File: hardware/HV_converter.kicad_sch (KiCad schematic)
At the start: 26 parts, among them J6 HV_IN, J7 HV_IN, J8 HV_THERM, U7 CN150B110-12, U8 LTV-817

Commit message: switch to pc
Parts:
- J8: footprint LHRS_Connectors:105313-2102 -> Connector_Molex:Molex_Nano-Fit_105309-xx02_1x02_P2.50mm_Vertical
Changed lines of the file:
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@@
 			)
 		)
-		(property "Footprint" "LHRS_Connectors:105313-2102"
+		(property "Footprint" "Connector_Molex:Molex_Nano-Fit_105309-xx02_1x02_P2.50mm_Vertical"
 			(at 66.04 147.32 0)
 			(hide yes)

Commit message: switch, stll working
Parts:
- TP20, TP21: footprint TestPoint:TestPoint_THTPad_D3.0mm_Drill1.5mm -> TestPoint:TestPoint_Loop_D2.50mm_Drill1.0mm_LowProfile
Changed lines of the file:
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@@
 			)
 		)
-		(property "Footprint" "TestPoint:TestPoint_THTPad_D3.0mm_Drill1.5mm"
+		(property "Footprint" "TestPoint:TestPoint_Loop_D2.50mm_Drill1.0mm_LowProfile"
 			(at 194.31 125.73 0)
 			(hide yes)
@@
 			)
 		)
-		(property "Footprint" "TestPoint:TestPoint_THTPad_D3.0mm_Drill1.5mm"
+		(property "Footprint" "TestPoint:TestPoint_Loop_D2.50mm_Drill1.0mm_LowProfile"
 			(at 194.31 138.43 0)
 			(hide yes)

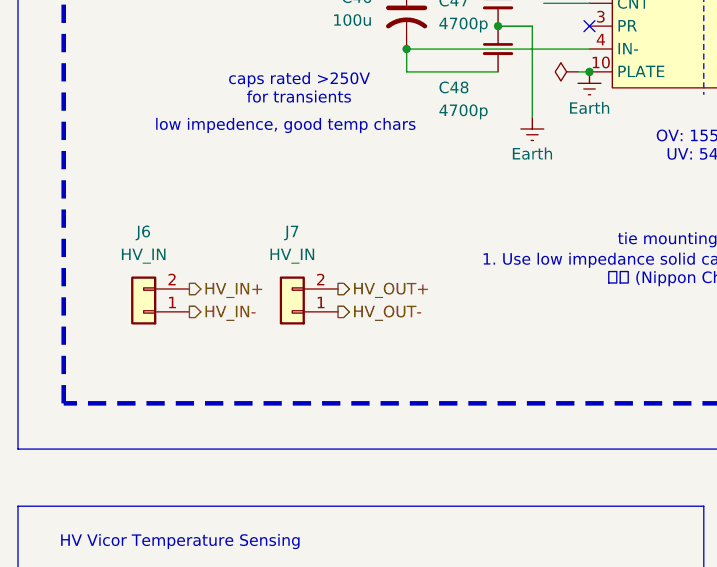
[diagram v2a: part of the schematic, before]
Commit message: switch to laptop
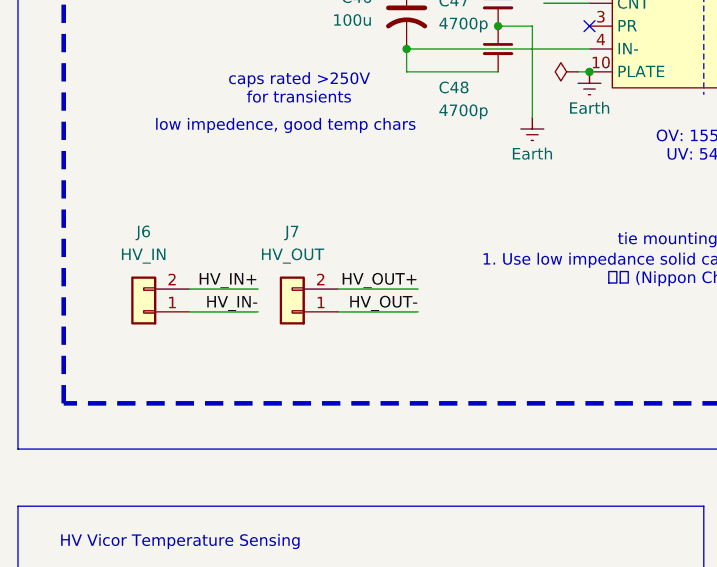
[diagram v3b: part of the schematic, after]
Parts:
- C53: footprint Capacitor_SMD:C_1812_4532Metric_Pad1.57x3.40mm_HandSolder -> Capacitor_SMD:CP_Elec_10x10.5; LCSC P/N C1812C204KAGLCAUTO -> C2980167
- J7: value HV_IN -> HV_OUT
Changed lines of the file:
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@@
+	(wire
+		(pts
+			(xy 45.72 77.47) (xy 38.1 77.47)
+		)
+		(stroke
+			(width 0)
+			(type default)
+		)
+	)
 	(wire
 		(pts
@@
 	(wire
 		(pts
+			(xy 63.5 80.01) (xy 54.61 80.01)
+		)
+		(stroke
+			(width 0)
+			(type default)
+		)
+	)
+	(wire
+		(pts
 			(xy 77.47 45.72) (xy 82.55 45.72)
 		)
@@
 	(wire
 		(pts
+			(xy 63.5 77.47) (xy 54.61 77.47)
+		)
+		(stroke
+			(width 0)
+			(type default)
+		)
+	)
+	(wire
+		(pts
 			(xy 107.95 43.18) (xy 116.84 43.18)
 		)
@@
 	(wire
 		(pts
+			(xy 45.72 80.01) (xy 38.1 80.01)
+		)
+		(stroke
+			(width 0)
+			(type default)
+		)
+	)
+	(wire
+		(pts
 			(xy 54.61 161.29) (xy 54.61 154.94)
 		)
@@
 			(width 0)
 			(type default)
+		)
+	)
+	(label "HV_OUT-"
+		(at 63.5 80.01 180)
+		(effects
+			(font
+				(size 1.27 1.27)
+			)
+			(justify right bottom)
 		)
 	)
@@
 		)
 	)
+	(label "HV_OUT+"
+		(at 63.5 77.47 180)
+		(effects
+			(font
+				(size 1.27 1.27)
+			)
+			(justify right bottom)
+		)
+	)
 	(label "HV_OUT_V"
 		(at 227.33 52.07 0)
@@
 		)
 	)
+	(label "HV_IN+"
+		(at 45.72 77.47 180)
+		(effects
+			(font
+				(size 1.27 1.27)
+			)
+			(justify right bottom)
+		)
+	)
+	(label "HV_IN-"
+		(at 45.72 80.01 180)
+		(effects
+			(font
+				(size 1.27 1.27)
+			)
+			(justify right bottom)
+		)
+	)
 	(label "HV_OUT_I"
 		(at 227.33 49.53 0)
@@
 			)
 			(justify left bottom)
-		)
-	)
-	(hierarchical_label "HV_IN-"
-		(shape output)
-		(at 38.1 80.01 0)
-		(effects
-			(font
-				(size 1.27 1.27)
-			)
-			(justify left)
 		)
 	)
@@
 		)
 	)
-	(hierarchical_label "HV_OUT+"
-		(shape output)
-		(at 54.61 77.47 0)
-		(effects
-			(font
-				(size 1.27 1.27)
-			)
-			(justify left)
-		)
-	)
 	(hierarchical_label "LV_GND"
 		(shape input)
@@
 		)
 	)
-	(hierarchical_label "HV_OUT-"
-		(shape output)
-		(at 54.61 80.01 0)
-		(effects
-			(font
-				(size 1.27 1.27)
-			)
-			(justify left)
-		)
-	)
 	(hierarchical_label "HV_24V_OUT"
 		(shape output)
 		(at 189.23 128.27 0)
-		(effects
-			(font
-				(size 1.27 1.27)
-			)
-			(justify left)
-		)
-	)
-	(hierarchical_label "HV_IN+"
-		(shape output)
-		(at 38.1 77.47 0)
 		(effects
 			(font
@@
 			)
 		)
-		(property "Value" "HV_IN"
+		(property "Value" "HV_OUT"
 			(at 49.53 73.66 0)
 			(show_name no)
@@
 			)
 		)
-		(property "Footprint" "Capacitor_SMD:C_1812_4532Metric_Pad1.57x3.40mm_HandSolder"
+		(property "Footprint" "Capacitor_SMD:CP_Elec_10x10.5"
 			(at 143.2052 52.07 0)
 			(hide yes)
@@
 			)
 		)
-		(property "LCSC P/N" "C1812C204KAGLCAUTO"
+		(property "LCSC P/N" "C2980167"
 			(at 142.24 48.26 0)
 			(hide yes)

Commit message: switch to pc...
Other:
- sheet Voltage + Current Sense ports: added VS; removed none
- moved on the sheet: TP20, TP21
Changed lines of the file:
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@@
 	(wire
 		(pts
+			(xy 226.06 40.64) (xy 229.87 40.64)
+		)
+		(stroke
+			(width 0)
+			(type default)
+		)
+	)
+	(wire
+		(pts
 			(xy 60.96 138.43) (xy 60.96 147.32)
 		)
@@
 	(wire
 		(pts
-			(xy 189.23 125.73) (xy 189.23 128.27)
+			(xy 196.85 125.73) (xy 196.85 128.27)
 		)
 		(stroke
@@
 	(wire
 		(pts
-			(xy 189.23 138.43) (xy 189.23 139.7)
+			(xy 196.85 138.43) (xy 196.85 139.7)
 		)
 		(stroke
@@
 		)
 	)
+	(hierarchical_label "VS"
+		(shape input)
+		(at 229.87 40.64 0)
+		(effects
+			(font
+				(size 1.27 1.27)
+			)
+			(justify left)
+		)
+	)
 	(hierarchical_label "HV_IN"
-		(shape output)
+		(shape input)
 		(at 52.07 43.18 180)
 		(effects
@@
 	(hierarchical_label "HV_24V_OUT"
 		(shape output)
-		(at 189.23 128.27 0)
+		(at 196.85 128.27 0)
 		(effects
 			(font
@@
 	(symbol
 		(lib_id "power:Earth")
-		(at 189.23 139.7 0)
+		(at 196.85 139.7 0)
 		(unit 1)
 		(body_style 1)
@@
 		(dnp no)
 		(property "Reference" "#PWR029"
-			(at 189.23 146.05 0)
+			(at 196.85 146.05 0)
 			(hide yes)
 			(show_name no)
@@
 		)
 		(property "Value" "Earth"
-			(at 189.23 143.764 0)
+			(at 196.85 143.764 0)
 			(show_name no)
 			(do_not_autoplace no)
@@
 		)
 		(property "Footprint" ""
-			(at 189.23 139.7 0)
+			(at 196.85 139.7 0)
 			(hide yes)
 			(show_name no)
@@
 		)
 		(property "Datasheet" ""
-			(at 189.23 139.7 0)
+			(at 196.85 139.7 0)
 			(hide yes)
 			(show_name no)
@@
 		)
 		(property "Description" "Power symbol creates a global label with name \"Earth\""
-			(at 189.23 139.7 0)
+			(at 196.85 139.7 0)
 			(hide yes)
 			(show_name no)
@@
 	(symbol
 		(lib_id "Connector:TestPoint")
-		(at 189.23 125.73 0)
+		(at 196.85 125.73 0)
 		(unit 1)
 		(body_style 1)
@@
 		(fields_autoplaced yes)
 		(property "Reference" "TP20"
-			(at 191.77 121.1579 0)
+			(at 199.39 121.1579 0)
 			(show_name no)
 			(do_not_autoplace no)
@@
 		)
 		(property "Value" "HV_24V_OUT"
-			(at 191.77 123.6979 0)
+			(at 199.39 123.6979 0)
 			(show_name no)
 			(do_not_autoplace no)
@@
 		)
 		(property "Footprint" "TestPoint:TestPoint_Loop_D2.50mm_Drill1.0mm_LowProfile"
-			(at 194.31 125.73 0)
+			(at 201.93 125.73 0)
 			(hide yes)
 			(show_name no)
@@
 		)
 		(property "Datasheet" ""
-			(at 194.31 125.73 0)
+			(at 201.93 125.73 0)
 			(hide yes)
 			(show_name no)
@@
 		)
 		(property "Description" "test point"
-			(at 189.23 125.73 0)
+			(at 196.85 125.73 0)
 			(hide yes)
 			(show_name no)
@@
 		)
 		(property "LCSC" ""
-			(at 189.23 125.73 0)
+			(at 196.85 125.73 0)
 			(hide yes)
 			(show_name no)
@@
 	(symbol
 		(lib_id "Connector:TestPoint")
-		(at 189.23 138.43 0)
+		(at 196.85 138.43 0)
 		(unit 1)
 		(body_style 1)
@@
 		(fields_autoplaced yes)
 		(property "Reference" "TP21"
-			(at 191.77 133.8579 0)
+			(at 199.39 133.8579 0)
 			(show_name no)
 			(do_not_autoplace no)
@@
 		)
 		(property "Value" "Earf"
-			(at 191.77 136.3979 0)
+			(at 199.39 136.3979 0)
 			(show_name no)
 			(do_not_autoplace no)
@@
 		)
 		(property "Footprint" "TestPoint:TestPoint_Loop_D2.50mm_Drill1.0mm_LowProfile"
-			(at 194.31 138.43 0)
+			(at 201.93 138.43 0)
 			(hide yes)
 			(show_name no)
@@
 		)
 		(property "Datasheet" ""
-			(at 194.31 138.43 0)
+			(at 201.93 138.43 0)
 			(hide yes)
 			(show_name no)
@@
 		)
 		(property "Description" "test point"
-			(at 189.23 138.43 0)
+			(at 196.85 138.43 0)
 			(hide yes)
 			(show_name no)
@@
 		)
 		(property "LCSC" ""
-			(at 189.23 138.43 0)
+			(at 196.85 138.43 0)
 			(hide yes)
 			(show_name no)
@@
 			(effects
 				(font
+					(size 1.27 1.27)
+				)
+				(justify right)
+			)
+		)
+		(pin "VS" input
+			(at 226.06 40.64 0)
+			(effects
+				(font

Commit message: switch to pc
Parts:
- removed J7: HV_OUT, LHRS_Connectors:AMASS_XT30UPB-M_1x02_P5.0mm_Vertical, symbol Connector_Generic:Conn_01x02
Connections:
- net HV_IN+ is gone; now on net OUT+: J6.2 (Pin_2)
- net HV_IN- is gone; now on net LV_GND: J6.1 (Pin_1)

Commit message: oops
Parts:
- C45, C49: P/N (none) -> MLASH168SB7104KTNA01
- R53: value R -> 0
- R54: LCSC P/N (none) -> C49330142; P/N (none) -> AST03330RJ
- U8: P/N (none) -> LTV-817-A
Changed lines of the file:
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@@
+			)
+		)
+		(property "P/N" "MLASH168SB7104KTNA01"
+			(at 48.26 147.32 0)
+			(hide yes)
+			(show_name no)
+			(do_not_autoplace no)
+			(effects
+				(font
+					(size 1.27 1.27)
+				)
 			)
 		)
@@
 		)
 		(property "LCSC" ""
+			(at 130.81 135.89 0)
+			(hide yes)
+			(show_name no)
+			(do_not_autoplace no)
+			(effects
+				(font
+					(size 1.27 1.27)
+				)
+			)
+		)
+		(property "P/N" "LTV-817-A"
 			(at 130.81 135.89 0)
 			(hide yes)
@@
 			)
 		)
-		(property "Value" "R"
+		(property "Value" "0"
 			(at 113.03 52.07 90)
 			(show_name no)
@@
 			)
 		)
+		(property "LCSC P/N" "C49330142"
+			(at 140.97 133.35 90)
+			(hide yes)
+			(show_name no)
+			(do_not_autoplace no)
+			(effects
+				(font
+					(size 1.27 1.27)
+				)
+			)
+		)
+		(property "P/N" "AST03330RJ"
+			(at 140.97 133.35 90)
+			(hide yes)
+			(show_name no)
+			(do_not_autoplace no)
+			(effects
+				(font
+					(size 1.27 1.27)
+				)
+			)
+		)
 		(pin "1"
 		)
@@
 			(at 120.65 135.89 0)
 			(hide yes)
+			(show_name no)
+			(do_not_autoplace no)
+			(effects
+				(font
+					(size 1.27 1.27)
+				)
+			)
+		)
+		(property "P/N" "MLASH168SB7104KTNA01"
+			(at 120.65 135.89 0)
+			(hide yes)

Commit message: push to github *traumatized*
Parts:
- C47, C48: footprint Capacitor_SMD:C_0603_1608Metric_Pad1.08x0.95mm_HandSolder -> Capacitor_SMD:C_0805_2012Metric_Pad1.18x1.45mm_HandSolder; LCSC P/N C106218 -> C107168; P/N (none) -> CC0805KRX7RYBB472
- C50, C51: LCSC P/N C106218 -> C21122; P/N (none) -> 06035C223K4T4A
- C52: LCSC P/N C106218 -> (none)
- J8: footprint Connector_Molex:Molex_Nano-Fit_105309-xx02_1x02_P2.50mm_Vertical -> LHRS_Connectors:Molex_Nano-Fit_105309-xx02_1x02_P2.50mm_Vertical
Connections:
- no-connect marks 1 -> 0
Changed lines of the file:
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@@
 		(color 0 0 0 0)
 	)
-	(no_connect
-		(at 82.55 48.26)
-	)
 	(bus_entry
 		(at 236.22 52.07)
@@
 			)
 		)
-		(property "LCSC P/N" "C106218"
+		(property "LCSC P/N" ""
 			(at 137.16 48.26 0)
 			(hide yes)
@@
 			)
 		)
-		(property "LCSC P/N" "C106218"
+		(property "LCSC P/N" "C21122"
 			(at 124.46 50.8 0)
 			(hide yes)
@@
 			)
 		)
+		(property "P/N" "06035C223K4T4A "
+			(at 124.46 50.8 0)
+			(hide yes)
+			(show_name no)
+			(do_not_autoplace no)
+			(effects
+				(font
+					(size 1.27 1.27)
+				)
+			)
+		)
 		(pin "2"
 		)
@@
 			)
 		)
-		(property "Footprint" "Capacitor_SMD:C_0603_1608Metric_Pad1.08x0.95mm_HandSolder"
+		(property "Footprint" "Capacitor_SMD:C_0805_2012Metric_Pad1.18x1.45mm_HandSolder"
 			(at 72.39 45.72 0)
 			(hide yes)
@@
 			)
 		)
-		(property "LCSC P/N" "C106218"
+		(property "LCSC P/N" "C107168"
 			(at 72.39 45.72 0)
 			(hide yes)
@@
 			)
 		)
+		(property "P/N" "CC0805KRX7RYBB472"
+			(at 72.39 45.72 0)
+			(hide yes)
+			(show_name no)
+			(do_not_autoplace no)
+			(effects
+				(font
+					(size 1.27 1.27)
+				)
+			)
+		)
 		(pin "2"
 		)
@@
 			)
 		)
-		(property "LCSC P/N" "C106218"
+		(property "LCSC P/N" "C21122"
 			(at 124.46 45.72 0)
 			(hide yes)
@@
 			)
 		)
+		(property "P/N" "06035C223K4T4A "
+			(at 124.46 45.72 0)
+			(hide yes)
+			(show_name no)
+			(do_not_autoplace no)
+			(effects
+				(font
+					(size 1.27 1.27)
+				)
+			)
+		)
 		(pin "2"
 		)
@@
 		(pin "6"
 		)
-		(pin "3"
-		)
 		(pin "5"
 		)
@@
 			)
 		)
-		(property "Footprint" "Capacitor_SMD:C_0603_1608Metric_Pad1.08x0.95mm_HandSolder"
+		(property "Footprint" "Capacitor_SMD:C_0805_2012Metric_Pad1.18x1.45mm_HandSolder"
 			(at 72.39 50.8 0)
 			(hide yes)
@@
 			)
 		)
-		(property "LCSC P/N" "C106218"
+		(property "LCSC P/N" "C107168"
 			(at 72.39 50.8 0)
 			(hide yes)
@@
 			)
 		)
+		(property "P/N" "CC0805KRX7RYBB472"
+			(at 72.39 50.8 0)
+			(hide yes)
+			(show_name no)
+			(do_not_autoplace no)
+			(effects
+				(font
+					(size 1.27 1.27)
+				)
+			)
+		)
 		(pin "2"
 		)
@@
 			)
 		)
-		(property "Footprint" "Connector_Molex:Molex_Nano-Fit_105309-xx02_1x02_P2.50mm_Vertical"
+		(property "Footprint" "LHRS_Connectors:Molex_Nano-Fit_105309-xx02_1x02_P2.50mm_Vertical"
 			(at 66.04 147.32 0)
 			(hide yes)

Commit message: added most p/n, still in progress but saving
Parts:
- C46: P/N (none) -> VKMI2102E101MV
- C52: LCSC P/N (none) -> C57895; P/N (none) -> CL10A225KA8NNNC
- C53: P/N (none) -> GVT1E681M1010
- R51, R56, R57: Assemble (none) -> -- mixed values --; Mouser Part Number (none) -> -- mixed values --; P/N (none) -> -- mixed values --
- R52: LCSC P/N (none) -> C21189; Manufacturer_Part_Number (none) -> -- mixed values --; P/N (none) -> CRCW06030000Z0EE
- R53: LCSC P/N (none) -> C21189; Manufacturer_Part_Number (none) -> -- mixed values --; P/N (none) -> CRCW06030000Z0EE; now fitted
- R55: Assemble (none) -> -- mixed values --; LCSC P/N (none) -> C25803; P/N (none) -> CRCW0603100KFKEE
